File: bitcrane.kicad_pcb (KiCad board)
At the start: 4 copper layers, 110 x 100 mm, 76 parts, among them J1 PSU Comm, J10 61900411021, J2 Hashboard0, J3 0455580003, J4 61900411021, J5 61900411021, J6 USB_C_Receptacle_USB2.0, J7 0353180420, J8 0353180420, J9 61900411021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

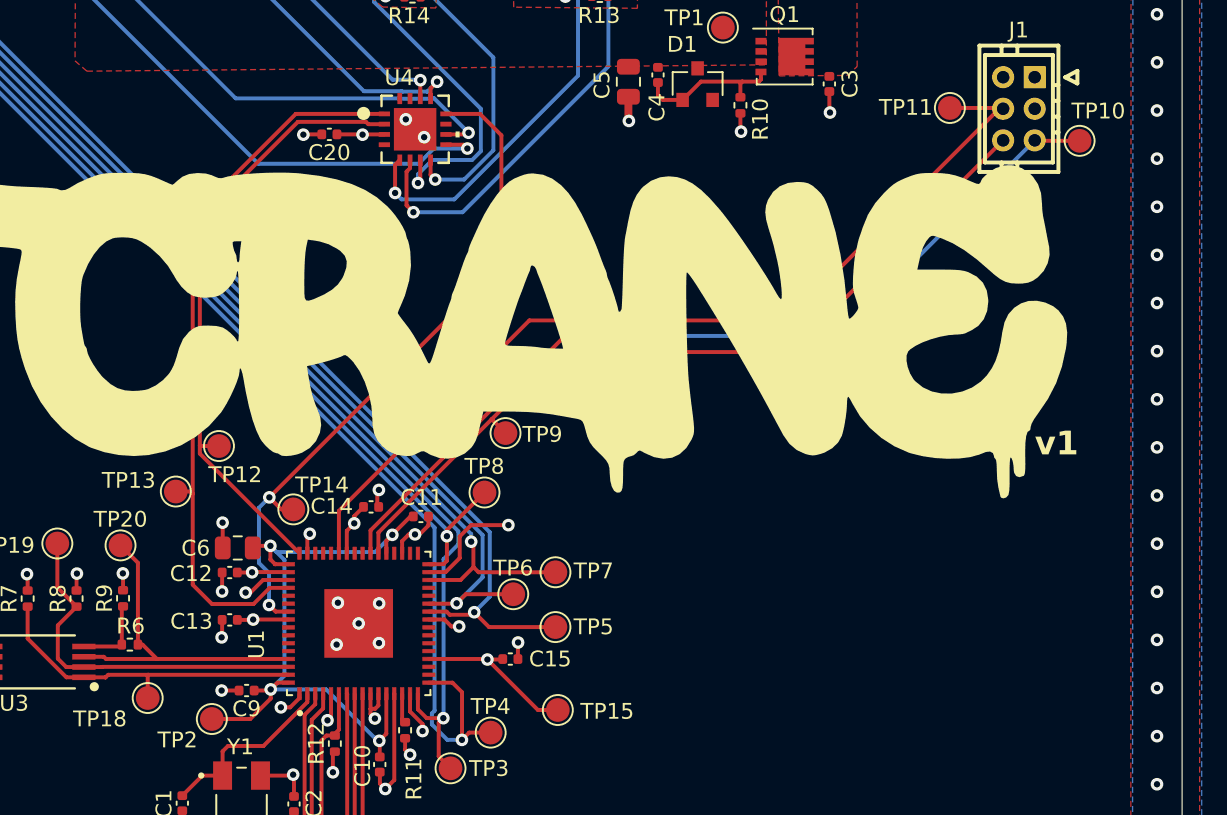
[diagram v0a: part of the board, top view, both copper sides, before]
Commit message: added fixes for #2 #3 #4 to schematic. still needs to be adjusted in layout
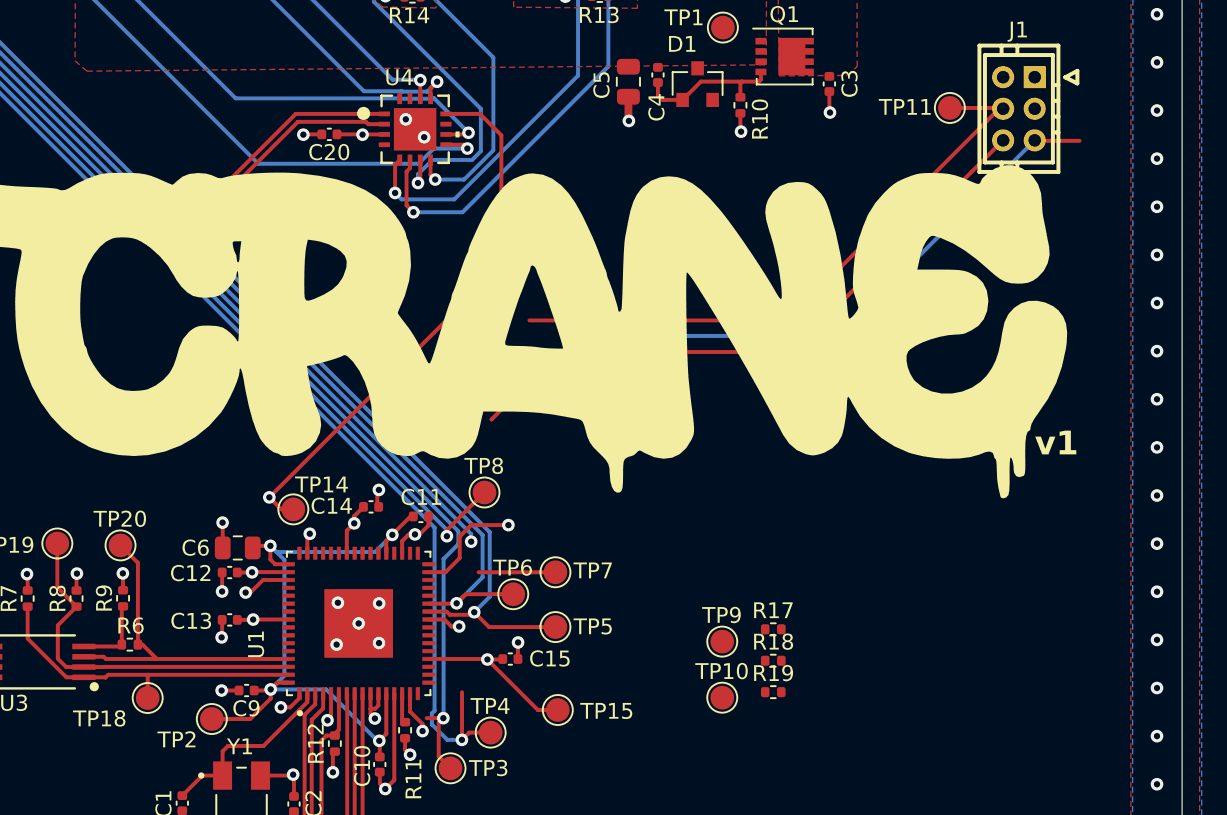
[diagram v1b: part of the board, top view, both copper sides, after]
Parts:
- removed TP12, TP13: TestPoint, TestPoint:TestPoint_Pad_D1.5mm
- added R17: 33k, Resistor_SMD:R_0402_1005Metric, F.Cu at (142.4, 97.5)
- added R18: 22k, Resistor_SMD:R_0402_1005Metric, F.Cu at (142.4, 99.5)
- added R19: 4.7k, Resistor_SMD:R_0402_1005Metric, F.Cu at (142.4, 101.5)
- moved TP10 41.9 mm to (139.2, 101.9)
- moved TP9 19.0 mm to (139.2, 98.3)
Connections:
- J1 pad 3: /PSU_SDA -> /SDA
- J1 pad 6: /PSU_SCL -> /SCL
- J2 pad 3: /SDA -> /HB_SDA
- J2 pad 4: /SCL -> /HB_SCL
- TP10 pad 1: /PSU_SDA -> /HB_SDA
- TP9 pad 1: /PSU_SCL -> /HB_SCL
- U1 pad 16: /TXD -> /HB_SCL
- U1 pad 17: /RXD -> /HB_SDA
- U1 pad 18: unconnected-(U1-ADBUS2-Pad18) -> /HB_SDA
- U1 pad 19: unconnected-(U1-ADBUS3-Pad19) -> /PLUG
- U1 pad 21: unconnected-(U1-ADBUS4-Pad21) -> /RST
- U1 pad 28: unconnected-(U1-BDBUS2-Pad28) -> /SDA
- U1 pad 30: /PLUG -> /FAN_ALERT
- U1 pad 32: /RST -> /PSU_EN
- U1 pad 38: /PSU_SCL -> /TXD
- U1 pad 39: /PSU_SDA -> /RXD
- U1 pad 43: /PSU_EN -> unconnected-(U1-CDBUS4-Pad43)
- U1 pad 48: /FAN_SCL -> unconnected-(U1-DDBUS0-Pad48)
- U1 pad 52: /FAN_SDA -> unconnected-(U1-DDBUS1-Pad52)
- U1 pad 55: /FAN_ALERT -> unconnected-(U1-DDBUS4-Pad55)
- U4 pad 1: /FAN_SDA -> /SDA
- U4 pad 11: unconnected-(U4-CLK-Pad11) -> Net-(U4-CLK)
- U4 pad 2: /FAN_SCL -> /SCL
- U4 pad 4: unconnected-(U4-ADDR_SEL-Pad4) -> Net-(U4-ADDR_SEL)
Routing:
- net /PSU_SDA: track 56.6 -> 0.00 mm, vias 1 -> 0
- net /SCL: track 83.6 -> 137.6 mm
- net /SDA: track 70.8 -> 123.4 mm, vias 1 -> 2
- net /PSU_SCL: track 52.4 -> 0.00 mm
- net /FAN_SDA: track 46.2 -> 0.00 mm
- net /FAN_SCL: track 39.2 -> 0.00 mm
- net /PSU_EN: track 58.7 -> 38.9 mm
- net /FAN_ALERT: track 43.7 -> 34.9 mm, vias 2 -> 1
- net /PLUG: track 72.2 -> 67.1 mm
- net /RST: track 74.0 -> 71.2 mm
- net /RXD: track 110.8 -> 108.5 mm
- net /TXD: track 82.5 -> 80.7 mm

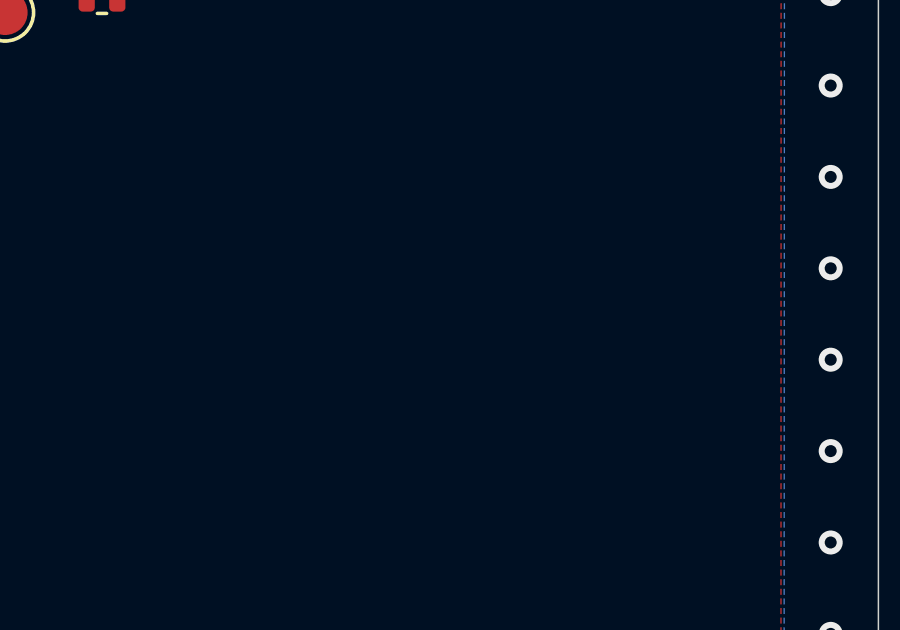
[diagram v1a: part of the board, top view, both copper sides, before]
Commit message: added fix for #5 to schematic. still needs PCB work
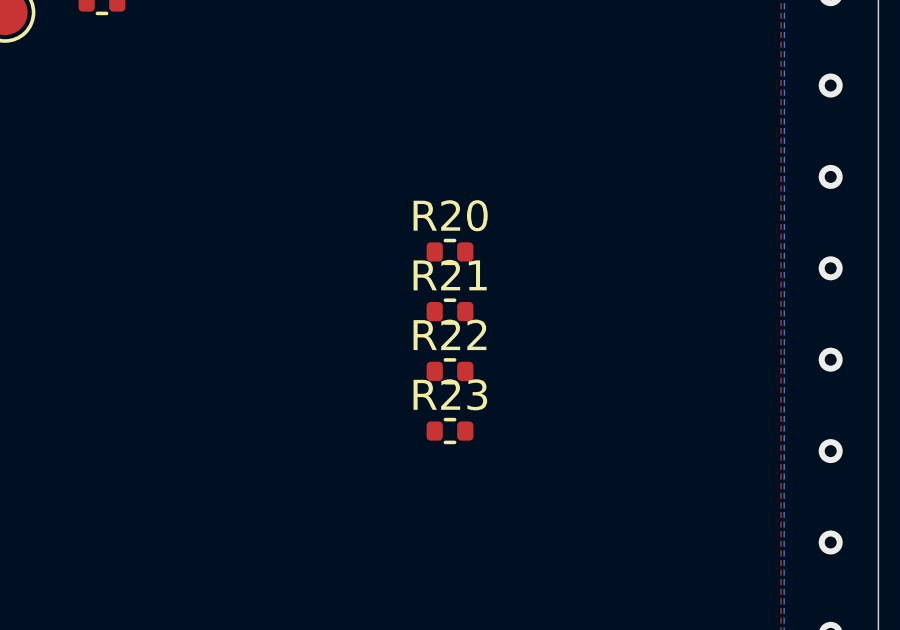
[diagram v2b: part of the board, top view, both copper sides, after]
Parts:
- added R20: 4.7K, Resistor_SMD:R_0402_1005Metric, F.Cu at (154.0, 109.8)
- added R21: 4.7K, Resistor_SMD:R_0402_1005Metric, F.Cu at (154.0, 111.8)
- added R22: 4.7K, Resistor_SMD:R_0402_1005Metric, F.Cu at (154.0, 113.8)
- added R23: 4.7K, Resistor_SMD:R_0402_1005Metric, F.Cu at (154.0, 115.8)

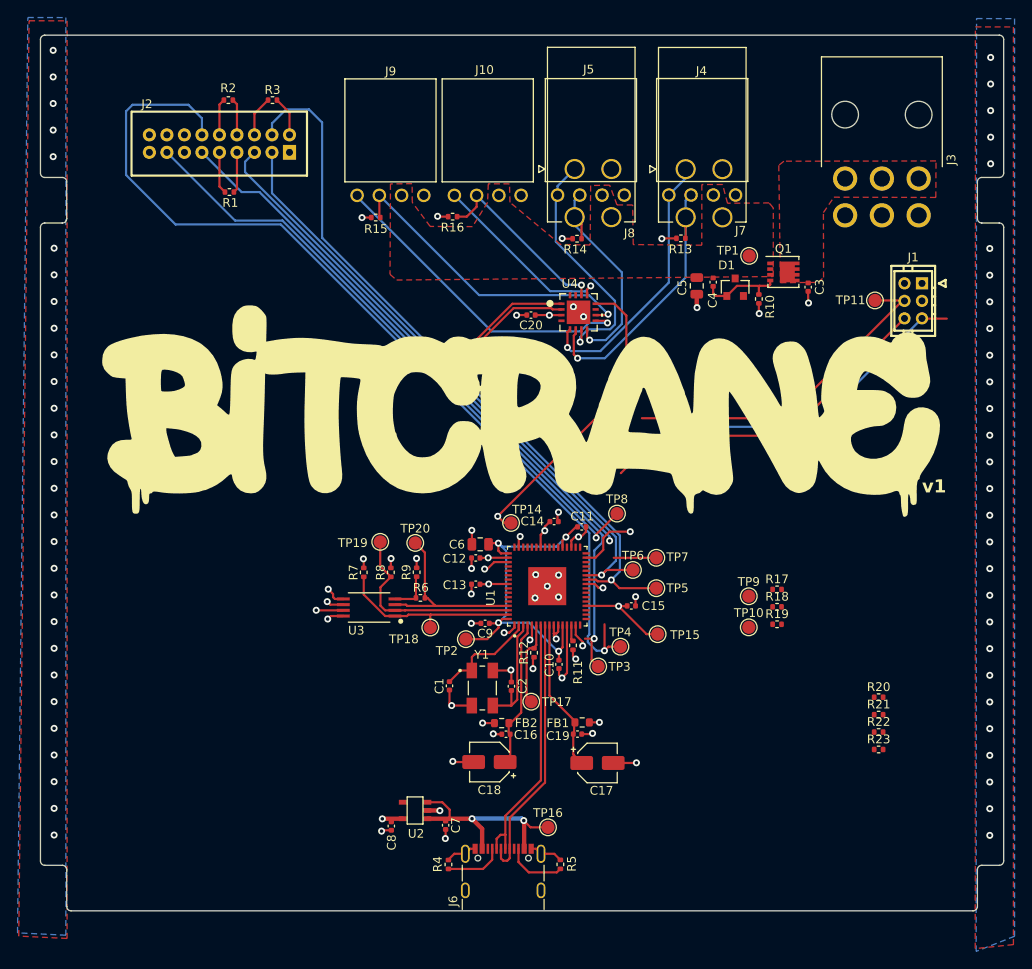
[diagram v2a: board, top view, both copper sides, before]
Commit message: routed v2 changes
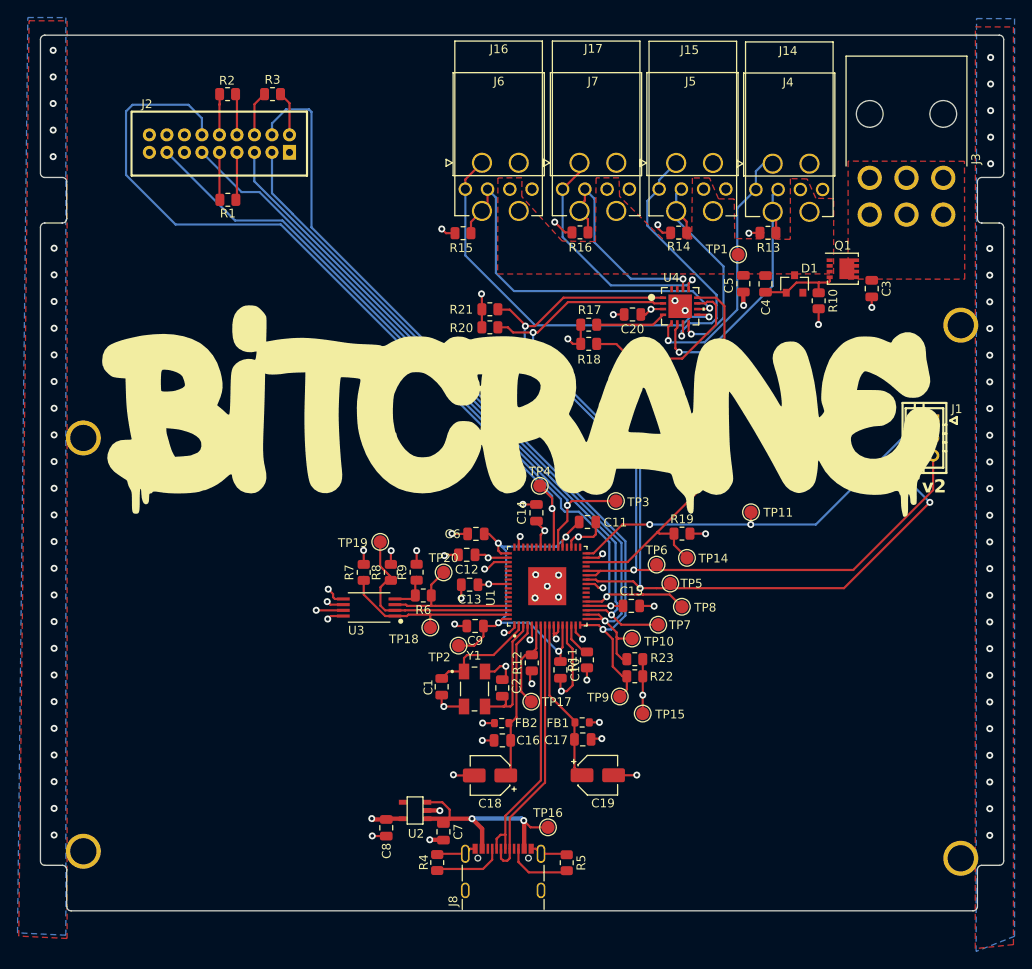
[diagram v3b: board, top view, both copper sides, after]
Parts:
- added H1: MountingHole_Pad, bitcrane:MountingHole_3mm_Pad, F.Cu at (163.4, 67.4)
- added H2: MountingHole_Pad, bitcrane:MountingHole_3mm_Pad, F.Cu at (163.4, 128.2)
- added H3: MountingHole_Pad, bitcrane:MountingHole_3mm_Pad, F.Cu at (63.2, 80.2)
- added H4: MountingHole_Pad, bitcrane:MountingHole_3mm_Pad, F.Cu at (63.2, 127.4)
- added J16: 0353180420, bitcrane:MOLEX_353180420, F.Cu at (108.7, 48.8)
- added J17: 0353180420, bitcrane:MOLEX_353180420, F.Cu at (119.8, 48.8)
- C1, C10, C11, C12, C13, C14, C15, C16, C17, C2, C20, C3, C4, C7, C8, C9: footprint Capacitor_SMD:C_0402_1005Metric -> Capacitor_SMD:C_0805_2012Metric
- R1, R10, R11, R12, R13, R14, R15, R16, R17, R18, R19, R2, R20, R21, R22, R23, R3, R4, R5, R6, R7, R8, R9: footprint Resistor_SMD:R_0402_1005Metric -> Resistor_SMD:R_0805_2012Metric
- U1: value FT4232HQ-REEL -> FT4232HQ
- U4: value EMC2305-1-AP-TR -> EMC2305
- moved R21 64.1 mm to (109.6, 65.5), turned to 180 degrees
- moved R20 61.3 mm to (109.6, 67.6), turned to 180 degrees
- moved R17 37.1 mm to (120.9, 67.3), turned to 180 degrees
- moved R18 36.9 mm to (120.9, 69.5), turned to 180 degrees
- moved R23 29.7 mm to (126.1, 105.5)
- moved R22 28.6 mm to (126.1, 107.5)
- moved TP11 28.0 mm to (139.4, 88.7)
- moved TP4 20.5 mm to (115.3, 85.7)
- moved TP14 20.5 mm to (132.1, 93.9)
- moved TP3 19.0 mm to (124.0, 87.5)
- moved TP9 18.7 mm to (124.4, 109.8)
- moved J1 15.7 mm to (159.2, 80.2)
- moved R19 15.0 mm to (131.5, 91.2)
- moved R16 14.7 mm to (119.9, 56.8)
- moved TP10 13.4 mm to (125.8, 103.2)
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- renumbered J7 to J14, J8 to J15, J9 to J6, J10 to J7, J6 to J8
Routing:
- net /HB_SCL: track 0.00 -> 94.4 mm, vias 0 -> 1
- net /HB_SDA: track 0.00 -> 83.7 mm, vias 0 -> 1
- net /SCL: track 137.6 -> 104.6 mm, vias 1 -> 3
- net Net-(U4-CLK): track 0.00 -> 20.4 mm
- net /SDA: track 123.4 -> 103.5 mm
- net /RXD: track 108.5 -> 91.7 mm
- net /RST: track 71.2 -> 87.8 mm
- net /FAN_ALERT: track 34.9 -> 47.4 mm, vias 1 -> 0
- net GND: track 85.4 -> 97.5 mm
- net /PLUG: track 67.1 -> 79.2 mm
- net VCCIO: track 48.7 -> 60.4 mm, vias 19 -> 23
- net /TXD: track 80.7 -> 69.8 mm
- net Net-(U4-ADDR_SEL): track 0.00 -> 8.05 mm
- net Net-(J16-Pin_4): track 37.0 -> 44.4 mm
- net Net-(J16-Pin_3): track 35.8 -> 43.2 mm
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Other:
- board text added: "v2"
- board text removed: "v1"
